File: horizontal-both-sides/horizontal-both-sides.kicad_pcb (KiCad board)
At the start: 2 copper layers, 10.2 x 15.3 mm, 3 parts, among them J1 Grove-I2C-connector, J2 Conn_01x04, J3 Conn_01x04

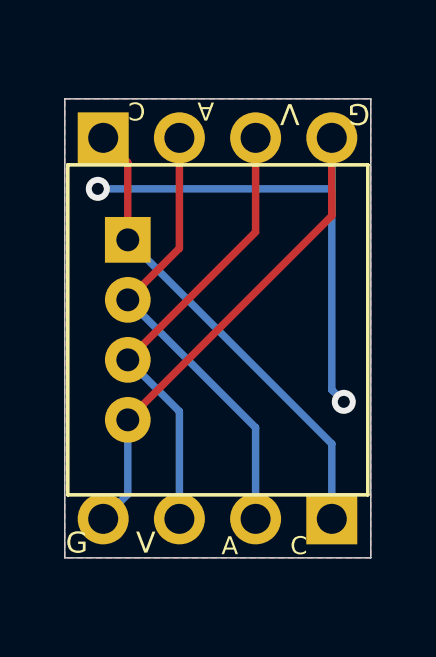
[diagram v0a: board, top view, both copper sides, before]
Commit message: Update silk lines for rev2021.02
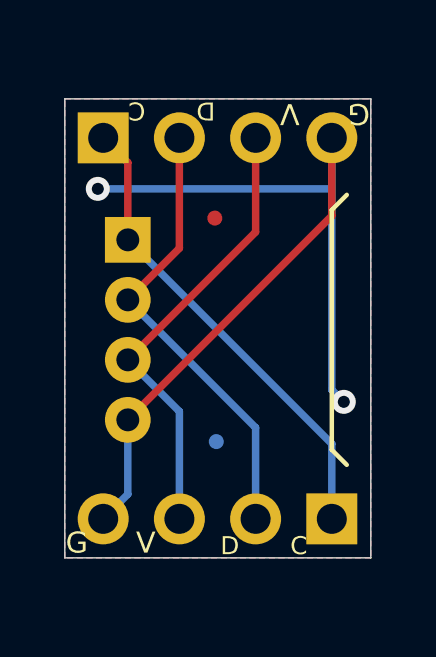
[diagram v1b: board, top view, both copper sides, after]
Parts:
- added fid1: Fiducial_0.5mm_Mask1mm, Fiducial:Fiducial_0.5mm_Mask1mm, F.Cu at (120.7, 67.9)
- added fid2: Fiducial_0.5mm_Mask1mm, Fiducial:Fiducial_0.5mm_Mask1mm, B.Cu at (120.8, 75.3)
- J1: footprint my-kicad-footprints:NS-Tech_Grove_1x04_P2mm_Horizontal -> my-kicad-footprints:NS-Tech_Grove_1x04_P2mm_Horizontal_silk_inside
- J2, J3: footprint Connector_PinHeader_2.54mm:PinHeader_1x04_P2.54mm_Vertical -> my-kicad-footprints:PinHeader_1x04_P2.54mm_Vertical_silk_inside
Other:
- board text added: "D"
- board text added: "Rev2021.02"
- board text removed: "A"
- board text removed: "Rev2020.12"
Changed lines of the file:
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@@
-(kicad_pcb (version 20171130) (host pcbnew 5.1.7-a382d34a8~87~ubuntu20.04.1)
+(kicad_pcb (version 20171130) (host pcbnew 5.1.9-73d0e3b20d~88~ubuntu20.04.1)
   (general
     (thickness 1.6)
@@
     (tracks 22)
     (zones 0)
-    (modules 3)
+    (modules 5)
     (nets 5)
   )
@@
     (add_net "Net-(J1-Pad3)")
   )
-  (module Connector_PinHeader_2.54mm:PinHeader_1x04_P2.54mm_Vertical (layer B.Cu)
+  (module Fiducial:Fiducial_0.5mm_Mask1mm (layer B.Cu)
+    (at 120.75 75.325)
+    (descr "Circular Fiducial, 0.5mm bare copper, 1mm soldermask opening (Level C)")
+    (tags fiducial)
+    (attr smd)
+    (fp_text reference fid2 (at 0 1.5) (layer B.SilkS) hide
+      (effects (font (size 1 1) (thickness 0.15)) (justify mirror))
+    )
+    (fp_text value Fiducial_0.5mm_Mask1mm (at 0 -1.5) (layer B.Fab) hide
+      (effects (font (size 1 1) (thickness 0.15)) (justify mirror))
+    )
+    (fp_circle (center 0 0) (end 0.75 0) (layer B.CrtYd) (width 0.05))
+    (fp_circle (center 0 0) (end 0.5 0) (layer B.Fab) (width 0.1))
+    (fp_text user %R (at 0 0) (layer B.Fab)
+      (effects (font (size 0.2 0.2) (thickness 0.04)) (justify mirror))
+    )
+    (pad "" smd circle (at 0 0) (size 0.5 0.5) (layers B.Cu B.Mask)
+      (solder_mask_margin 0.25) (clearance 0.25))
+  )
+  (module Fiducial:Fiducial_0.5mm_Mask1mm (layer F.Cu)
+    (at 120.7 67.875)
+    (descr "Circular Fiducial, 0.5mm bare copper, 1mm soldermask opening (Level C)")
+    (tags fiducial)
+    (attr smd)
+    (fp_text reference fid1 (at 0 -1.5) (layer F.SilkS) hide
+      (effects (font (size 1 1) (thickness 0.15)))
+    )
+    (fp_text value Fiducial_0.5mm_Mask1mm (at 0 1.5) (layer F.Fab) hide
+      (effects (font (size 1 1) (thickness 0.15)))
+    )
+    (fp_circle (center 0 0) (end 0.75 0) (layer F.CrtYd) (width 0.05))
+    (fp_circle (center 0 0) (end 0.5 0) (layer F.Fab) (width 0.1))
+    (fp_text user %R (at 0 0) (layer F.Fab)
+      (effects (font (size 0.2 0.2) (thickness 0.04)))
+    )
+    (pad "" smd circle (at 0 0) (size 0.5 0.5) (layers F.Cu F.Mask)
+      (solder_mask_margin 0.25) (clearance 0.25))
+  )
+  (module my-kicad-footprints:PinHeader_1x04_P2.54mm_Vertical_silk_inside (layer B.Cu)
     (at 116.98 65.2 270)
     (descr "Through hole straight pin header, 1x04, 2.54mm pitch, single row")
@@
       (effects (font (size 1 1) (thickness 0.15)) (justify mirror))
     )
-    (fp_text value Conn_01x04 (at 0 -9.95 90) (layer B.Fab)
-      (effects (font (size 1 1) (thickness 0.15)) (justify mirror))
-    )
+    (fp_text value Conn_01x04 (at 0 -9.95 90) (layer B.Fab) hide
+      (effects (font (size 1 1) (thickness 0.15)) (justify mirror))
+    )
+    (fp_line (start -0.635 1.27) (end 1.27 1.27) (layer B.Fab) (width 0.1))
+    (fp_line (start 1.27 1.27) (end 1.27 -8.89) (layer B.Fab) (width 0.1))
+    (fp_line (start 1.27 -8.89) (end -1.27 -8.89) (layer B.Fab) (width 0.1))
+    (fp_line (start -1.27 -8.89) (end -1.27 0.635) (layer B.Fab) (width 0.1))
+    (fp_line (start -1.27 0.635) (end -0.635 1.27) (layer B.Fab) (width 0.1))
+    (fp_line (start -1.03 -8.65) (end 1.03 -8.65) (layer B.SilkS) (width 0.12))
+    (fp_line (start -1.03 -0.3) (end -1.03 1.03) (layer B.SilkS) (width 0.12))
+    (fp_line (start -1.03 1.03) (end 0.3 1.03) (layer B.SilkS) (width 0.12))
+    (fp_line (start -1.8 1.8) (end -1.8 -9.4) (layer B.CrtYd) (width 0.05))
+    (fp_line (start -1.8 -9.4) (end 1.8 -9.4) (layer B.CrtYd) (width 0.05))
+    (fp_line (start 1.8 -9.4) (end 1.8 1.8) (layer B.CrtYd) (width 0.05))
     (fp_line (start 1.8 1.8) (end -1.8 1.8) (layer B.CrtYd) (width 0.05))
-    (fp_line (start 1.8 -9.4) (end 1.8 1.8) (layer B.CrtYd) (width 0.05))
-    (fp_line (start -1.8 -9.4) (end 1.8 -9.4) (layer B.CrtYd) (width 0.05))
-    (fp_line (start -1.8 1.8) (end -1.8 -9.4) (layer B.CrtYd) (width 0.05))
-    (fp_line (start -1.33 1.33) (end 0 1.33) (layer B.SilkS) (width 0.12))
-    (fp_line (start -1.33 0) (end -1.33 1.33) (layer B.SilkS) (width 0.12))
-    (fp_line (start -1.33 -1.27) (end 1.33 -1.27) (layer B.SilkS) (width 0.12))
-    (fp_line (start 1.33 -1.27) (end 1.33 -8.95) (layer B.SilkS) (width 0.12))
-    (fp_line (start -1.33 -1.27) (end -1.33 -8.95) (layer B.SilkS) (width 0.12))
-    (fp_line (start -1.33 -8.95) (end 1.33 -8.95) (layer B.SilkS) (width 0.12))
-    (fp_line (start -1.27 0.635) (end -0.635 1.27) (layer B.Fab) (width 0.1))
-    (fp_line (start -1.27 -8.89) (end -1.27 0.635) (layer B.Fab) (width 0.1))
-    (fp_line (start 1.27 -8.89) (end -1.27 -8.89) (layer B.Fab) (width 0.1))
-    (fp_line (start 1.27 1.27) (end 1.27 -8.89) (layer B.Fab) (width 0.1))
-    (fp_line (start -0.635 1.27) (end 1.27 1.27) (layer B.Fab) (width 0.1))
     (fp_text user %R (at 0 -3.81 180) (layer B.Fab)
       (effects (font (size 1 1) (thickness 0.15)) (justify mirror))
@@
     )
   )
-  (module Connector_PinHeader_2.54mm:PinHeader_1x04_P2.54mm_Vertical (layer B.Cu)
+  (module my-kicad-footprints:PinHeader_1x04_P2.54mm_Vertical_silk_inside (layer B.Cu)
     (at 124.6 77.9 90)
     (descr "Through hole straight pin header, 1x04, 2.54mm pitch, single row")
@@
       (effects (font (size 1 1) (thickness 0.15)) (justify mirror))
     )
-    (fp_text value Conn_01x04 (at 0 -9.95 90) (layer B.Fab)
-      (effects (font (size 1 1) (thickness 0.15)) (justify mirror))
-    )
+    (fp_text value Conn_01x04 (at 0 -9.95 90) (layer B.Fab) hide
+      (effects (font (size 1 1) (thickness 0.15)) (justify mirror))
+    )
+    (fp_line (start -0.635 1.27) (end 1.27 1.27) (layer B.Fab) (width 0.1))
+    (fp_line (start 1.27 1.27) (end 1.27 -8.89) (layer B.Fab) (width 0.1))
+    (fp_line (start 1.27 -8.89) (end -1.27 -8.89) (layer B.Fab) (width 0.1))
+    (fp_line (start -1.27 -8.89) (end -1.27 0.635) (layer B.Fab) (width 0.1))
+    (fp_line (start -1.27 0.635) (end -0.635 1.27) (layer B.Fab) (width 0.1))
+    (fp_line (start -1.03 -8.65) (end 1.03 -8.65) (layer B.SilkS) (width 0.12))
+    (fp_line (start -1.03 -0.3) (end -1.03 1.03) (layer B.SilkS) (width 0.12))
+    (fp_line (start -1.03 1.03) (end 0.3 1.03) (layer B.SilkS) (width 0.12))
+    (fp_line (start -1.8 1.8) (end -1.8 -9.4) (layer B.CrtYd) (width 0.05))
+    (fp_line (start -1.8 -9.4) (end 1.8 -9.4) (layer B.CrtYd) (width 0.05))
+    (fp_line (start 1.8 -9.4) (end 1.8 1.8) (layer B.CrtYd) (width 0.05))
     (fp_line (start 1.8 1.8) (end -1.8 1.8) (layer B.CrtYd) (width 0.05))
-    (fp_line (start 1.8 -9.4) (end 1.8 1.8) (layer B.CrtYd) (width 0.05))
-    (fp_line (start -1.8 -9.4) (end 1.8 -9.4) (layer B.CrtYd) (width 0.05))
-    (fp_line (start -1.8 1.8) (end -1.8 -9.4) (layer B.CrtYd) (width 0.05))
-    (fp_line (start -1.33 1.33) (end 0 1.33) (layer B.SilkS) (width 0.12))
-    (fp_line (start -1.33 0) (end -1.33 1.33) (layer B.SilkS) (width 0.12))
-    (fp_line (start -1.33 -1.27) (end 1.33 -1.27) (layer B.SilkS) (width 0.12))
-    (fp_line (start 1.33 -1.27) (end 1.33 -8.95) (layer B.SilkS) (width 0.12))
-    (fp_line (start -1.33 -1.27) (end -1.33 -8.95) (layer B.SilkS) (width 0.12))
-    (fp_line (start -1.33 -8.95) (end 1.33 -8.95) (layer B.SilkS) (width 0.12))
-    (fp_line (start -1.27 0.635) (end -0.635 1.27) (layer B.Fab) (width 0.1))
-    (fp_line (start -1.27 -8.89) (end -1.27 0.635) (layer B.Fab) (width 0.1))
-    (fp_line (start 1.27 -8.89) (end -1.27 -8.89) (layer B.Fab) (width 0.1))
-    (fp_line (start 1.27 1.27) (end 1.27 -8.89) (layer B.Fab) (width 0.1))
-    (fp_line (start -0.635 1.27) (end 1.27 1.27) (layer B.Fab) (width 0.1))
     (fp_text user %R (at 0 -3.81 180) (layer B.Fab)
       (effects (font (size 1 1) (thickness 0.15)) (justify mirror))
@@
     )
   )
-  (module my-kicad-footprints:NS-Tech_Grove_1x04_P2mm_Horizontal (layer F.Cu)
+  (module my-kicad-footprints:NS-Tech_Grove_1x04_P2mm_Horizontal_silk_inside (layer F.Cu)
     (at 117.8 71.6)
     (descr https://statics3.seeedstudio.com/images/opl/datasheet/3470130P1.pdf)
@@
       (effects (font (size 1 1) (thickness 0.15)))
     )
-    (fp_text value Grove-I2C-connector (at 9.1059 2.6924 90) (layer F.Fab)
-      (effects (font (size 1 1) (thickness 0.15)))
-    )
-    (fp_line (start -2 5.5) (end 8 5.5) (layer F.SilkS) (width 0.12))
-    (fp_line (start -2 -5.5) (end -2 5.5) (layer F.SilkS) (width 0.12))
-    (fp_line (start -2 -5.5) (end 8 -5.5) (layer F.SilkS) (width 0.12))
-    (fp_line (start 8 -5.5) (end 8 5.5) (layer F.SilkS) (width 0.12))
-    (fp_text user %R (at -2 -1 90) (layer F.Fab)
+    (fp_text value Grove-I2C-connector (at 9.1059 2.6924 90) (layer F.Fab) hide
+      (effects (font (size 1 1) (thickness 0.15)))
+    )
+    (fp_line (start 6.8 4) (end 7.3 4.5) (layer F.SilkS) (width 0.15))
+    (fp_line (start 6.8 -4) (end 6.8 4) (layer F.SilkS) (width 0.15))
+    (fp_line (start 7.3 -4.5) (end 6.8 -4) (layer F.SilkS) (width 0.15))
+    (fp_line (start -2 5.5) (end 8 5.5) (layer F.Fab) (width 0.12))
+    (fp_line (start -2 -5.5) (end -2 5.5) (layer F.Fab) (width 0.12))
+    (fp_line (start -2 -5.5) (end 8 -5.5) (layer F.Fab) (width 0.12))
+    (fp_line (start 8 -5.5) (end 8 5.5) (layer F.Fab) (width 0.12))
+    (fp_text user %R (at -2 -1 90) (layer F.Fab) hide
       (effects (font (size 1 1) (thickness 0.15)))
     )
@@
     (arrow2b (pts (xy 115.7 81.28) (xy 116.826504 80.693579)))
   )
-  (gr_text Rev2020.12 (at 119.6 76.4 270) (layer B.SilkS)
+  (gr_text Rev2021.02 (at 119.6 76.4 -90) (layer B.SilkS)
     (effects (font (size 0.6 0.6) (thickness 0.15)) (justify left mirror))
   )
@@
     (effects (font (size 0.6 0.6) (thickness 0.15)))
   )
-  (gr_text A (at 120.4 64.3 180) (layer F.SilkS)
+  (gr_text D (at 120.4 64.3 180) (layer F.SilkS)
     (effects (font (size 0.6 0.6) (thickness 0.15)))
   )
@@
     (effects (font (size 0.6 0.6) (thickness 0.15)))
   )
-  (gr_text A (at 121.2 78.8) (layer F.SilkS)
+  (gr_text D (at 121.2 78.8) (layer F.SilkS)
     (effects (font (size 0.6 0.6) (thickness 0.15)))
   )

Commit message: Update revision for bertical botn and one line and horizontal both
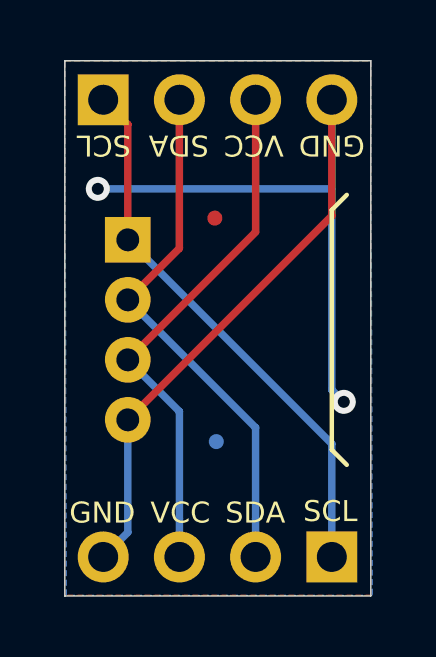
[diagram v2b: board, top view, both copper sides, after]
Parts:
- moved J3 1.27 mm to (117.0, 63.9)
- moved J2 1.27 mm to (124.6, 79.2)
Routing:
- net Net-(J1-Pad3): track 15.2 -> 17.7 mm
- net Net-(J1-Pad2): track 15.2 -> 17.7 mm
- net Net-(J1-Pad1): track 15.9 -> 18.4 mm
- net GND: track 34.3 -> 36.4 mm
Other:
- board size 10.2 x 15.3 mm -> 10.2 x 17.8 mm
- board text added: "GND"
- board text added: "Rev2021.04"
- board text added: "SCL"
- board text added: "SDA"
- board text added: "VCC"
- board text removed: "C"
- board text removed: "D"
- board text removed: "G"
- board text removed: "Rev2021.02"
- board text removed: "V"
